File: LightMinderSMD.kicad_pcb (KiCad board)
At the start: 2 copper layers, 49.5 x 23 mm, 39 parts, among them IC2 VN750PSTR-E, J1 Conn_01x06_Male, J2 AVR-ISP-6, J3 Conn_01x03, Q1 Q_NPN_BCE, U1 ATmega328P-AU, U2 LP2951-5.0_SOIC, Y1 Crystal_GND24

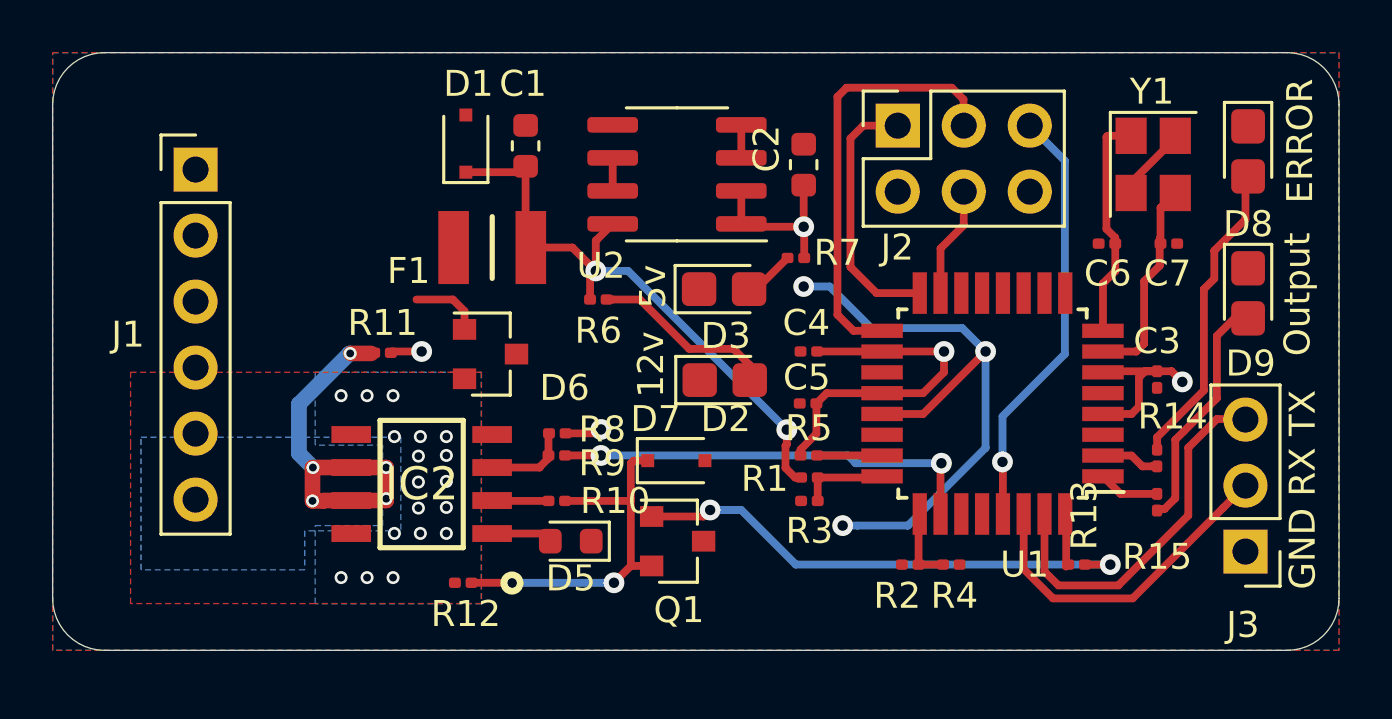
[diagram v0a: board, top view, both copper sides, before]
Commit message: Version 2 PCB fully routed, simulations added
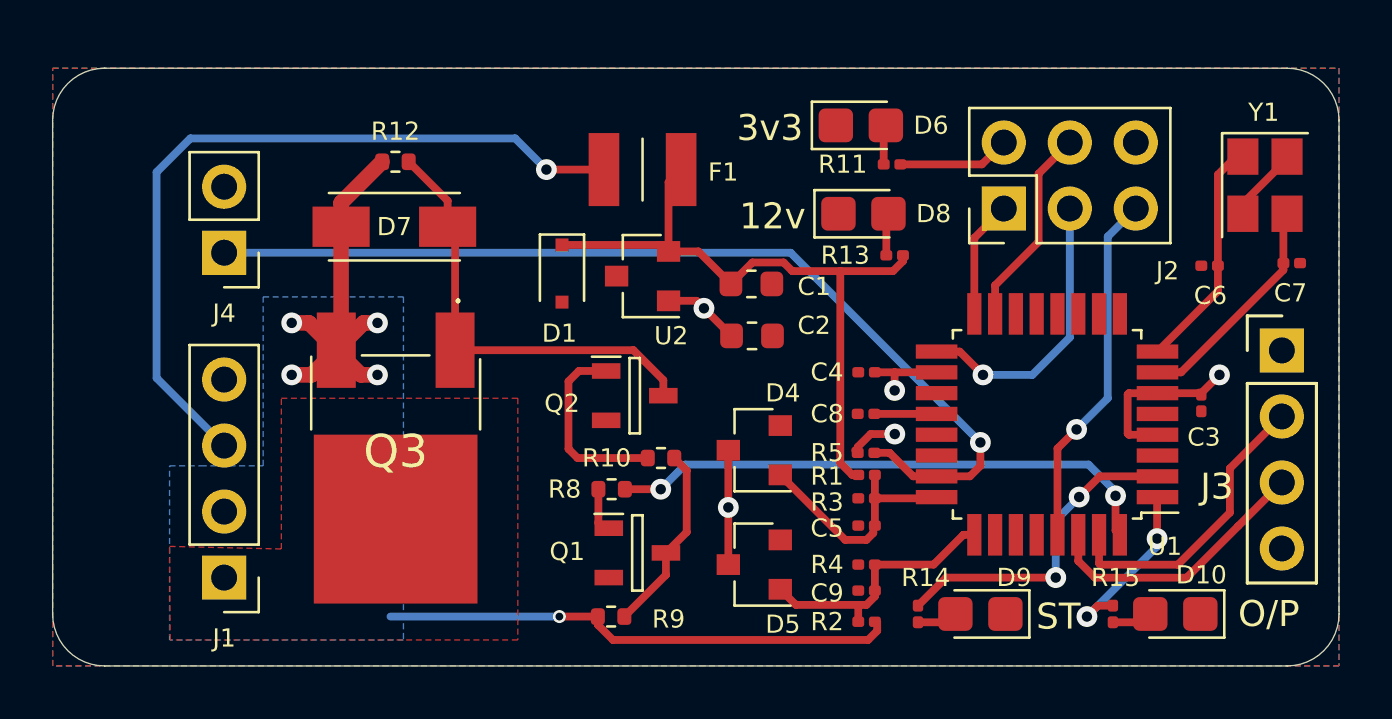
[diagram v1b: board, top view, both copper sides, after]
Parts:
- removed D2, D3: LED, LED_SMD:LED_0805_2012Metric_Castellated
- removed IC2: VN750PSTR-E, SamacSys_Parts:SOIC127P600X175-8N
- removed R6, R7: R, Resistor_SMD:R_0201_0603Metric
- added C8: 100n, Capacitor_SMD:C_0201_0603Metric, F.Cu at (124.3, 84.9)
- added C9: 470nF, Capacitor_SMD:C_0201_0603Metric, F.Cu at (124.3, 91.7)
- added D10: LED, LED_SMD:LED_0805_2012Metric_Castellated, F.Cu at (136.2, 92.6)
- added D4: D_Schottky, Diode_SMD:D_SOT-23_ANK, F.Cu at (120.0, 86.3)
- added J4: Conn_01x02_Female, Connector_PinHeader_2.54mm:PinHeader_1x02_P2.54mm_Vertical, F.Cu at (99.6, 78.7)
- added Q2: Q_NPN_BEC, SamacSys_Parts:SOT95P240X115-3N, F.Cu at (115.4, 84.2)
- added Q3: STD35P6LLF6, SamacSys_Parts:STD35P6LLF6, F.Cu at (106.2, 85.7)
- C1: value 1u -> 10u
- C2: value 4.7u -> 10u
- C5: value 100n -> 470nF
- D5: value D -> D_Schottky; footprint Diode_SMD:D_0603_1608Metric -> Diode_SMD:D_SOT-23_ANK
- D6: value D_TVS -> LED; footprint Diode_SMD:D_SOT-23_NKA -> LED_SMD:LED_0805_2012Metric_Castellated
- D7: value D_Zener -> 20v TVS; footprint Diode_SMD:D_SOD-323F -> SamacSys_Parts:DO-214ACSMA
- J1: value Conn_01x06_Male -> Conn_01x04_Female; footprint Connector_PinHeader_2.54mm:PinHeader_1x06_P2.54mm_Vertical -> Connector_PinHeader_2.54mm:PinHeader_1x04_P2.54mm_Vertical
- J2: footprint Connector_PinSocket_2.54mm:PinSocket_2x03_P2.54mm_Vertical -> Connector_PinHeader_2.54mm:PinHeader_2x03_P2.54mm_Vertical
- J3: value Conn_01x03 -> Conn_01x04; footprint Connector_PinHeader_2.54mm:PinHeader_1x03_P2.54mm_Vertical -> Connector_PinHeader_2.54mm:PinHeader_1x04_P2.54mm_Vertical
- Q1: value Q_NPN_BCE -> Q_NPN_BEC; footprint Package_TO_SOT_SMD:SOT-23 -> SamacSys_Parts:SOT95P240X115-3N
- R1, R2: value 15k -> 18k
- R10, R8: value 10k -> 1k; footprint Resistor_SMD:R_0201_0603Metric -> Resistor_SMD:R_0402_1005Metric
- R11: value 10k -> R
- R12: value 15k -> 10k; footprint Resistor_SMD:R_0201_0603Metric -> Resistor_SMD:R_0402_1005Metric
- R13: value 1k -> R
- R3, R4: value 5k1 -> 1.3k
- R9: footprint Resistor_SMD:R_0201_0603Metric -> Resistor_SMD:R_0402_1005Metric
- U2: value LP2951-5.0_SOIC -> LM3480-3.3; footprint Package_SO:SOIC-8_3.9x4.9mm_P1.27mm -> Package_TO_SOT_SMD:SOT-23
- moved R11 20.9 mm to (125.3, 75.3), turned to 180 degrees
- moved D6 16.7 mm to (124.1, 73.8)
- moved R12 16.4 mm to (106.2, 75.2)
- moved D9 16.1 mm to (128.7, 92.6), turned to 180 degrees
- moved J1 15.7 mm to (99.6, 91.2), turned to 180 degrees
- moved D8 15.0 mm to (124.2, 77.2), turned to 0 degrees
- moved D7 14.1 mm to (106.2, 77.7)
- moved R13 13.8 mm to (125.4, 78.8), turned to 180 degrees
- moved R14 11.0 mm to (126.3, 92.6), turned to 270 degrees
- moved C1 10.2 mm to (119.9, 79.9), turned to 0 degrees
- moved J3 7.87 mm to (140.3, 82.5), turned to 0 degrees
- moved D5 7.12 mm to (120.0, 90.7)
- moved C2 6.88 mm to (119.9, 81.9), turned to 0 degrees
- moved R9 6.54 mm to (114.5, 92.7), turned to 0 degrees
- moved F1 6.52 mm to (115.7, 75.5)
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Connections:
- net /Sheet60CB0BEF/11 renamed /Sheet60CB0BEF/MOSI
- net /Sheet60CB0BEF/12 renamed /Sheet60CB0BEF/MISO
- net /Sheet60CB0BEF/13 renamed /Sheet60CB0BEF/SCK
- C2 pad 1: 5v -> 3v3
- C3 pad 1: 5v -> 3v3
- C4 pad 1: 5v -> 3v3
- C5 pad 1: 5v -> /batt_voltage_ref
- D5 pad 1: Sidelight_GND -> 3v3
- D5 pad 2: Net-(D5-Pad2) -> /dipped_beam_ref
- D6 pad 1: DippedBeam_12v -> Sidelight_GND
- D6 pad 2: Sidelight_GND -> Net-(D6-Pad2)
- D7 pad 1: /Light_Control -> DippedBeam_12v
- D7 pad 2: Sidelight_GND -> Net-(D7-Pad2)
- J1 pad 1: Sidelight_GND -> DippedBeam_Out
- J1 pad 2: /Light_Ref -> DippedBeam_12v
- J1 pad 3: Sidelight_GND -> Sidelight_12v
- J1 pad 4: Sidelight_12v -> Sidelight_GND
- J2 pad 2: 5v -> 3v3
- J3 pad 2: /RX -> /TX
- J3 pad 3: /TX -> /RX
- Q1 pad 2: /Light_Control -> Sidelight_GND
- Q1 pad 3: Sidelight_GND -> Net-(Q1-Pad3)
- R1 pad 2: /Batt_Voltage_Ref -> /batt_voltage_ref
- R10 pad 1: Net-(IC2-Pad2) -> Net-(Q1-Pad3)
- R10 pad 2: /Light_Control -> Net-(Q2-Pad1)
- R11 pad 1: DippedBeam_Out -> 3v3
- R11 pad 2: 5v -> Net-(D6-Pad2)
- R12 pad 2: /Light_Control -> Net-(D7-Pad2)
- R13 pad 1: /Light_Out_Gate -> /12vFused
- R13 pad 2: Net-(Q1-Pad1) -> Net-(D8-Pad2)
- R14 pad 2: Net-(D8-Pad2) -> Net-(D9-Pad2)
- R15 pad 2: Net-(D9-Pad2) -> Net-(D10-Pad2)
- R2 pad 2: /Dipped_Beam_Ref -> /dipped_beam_ref
- R3 pad 1: /Batt_Voltage_Ref -> /batt_voltage_ref
- R4 pad 1: /Dipped_Beam_Ref -> /dipped_beam_ref
- R5 pad 1: 5v -> 3v3
- R5 pad 2: /Light_Ref -> /light_ref
- R8 pad 1: Net-(IC2-Pad3) -> /Light_Out_Logic
- R8 pad 2: 5v -> Net-(Q1-Pad1)
- R9 pad 1: /Status_In -> DippedBeam_12v
- R9 pad 2: Net-(IC2-Pad3) -> Net-(Q1-Pad3)
- U1 pad 18: 5v -> 3v3
- U1 pad 20: 5v -> /Sheet60CB0BEF/aref
- U1 pad 23: /Light_Ref -> /light_ref
- U1 pad 24: /Batt_Voltage_Ref -> /batt_voltage_ref
- U1 pad 25: /Dipped_Beam_Ref -> /dipped_beam_ref
- U1 pad 26: /Status_In -> /Sheet60CB0BEF/A3
- U1 pad 32: /Light_Out_Gate -> /Light_Out_Logic
- U1 pad 4: 5v -> 3v3
- U1 pad 6: 5v -> 3v3
- U2 pad 1: 5v -> 3v3
- U2 pad 2: 5v -> /12vFused
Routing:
- net /light_ref: track 0.00 -> 37.7 mm, vias 0 -> 1
- net DippedBeam_12v: track 0.00 -> 36.2 mm, vias 18 -> 5
- net Sidelight_12v: track 0.00 -> 29.8 mm, vias 0 -> 1
- net 5v: track 29.2 -> 0.00 mm, vias 5 -> 0
- net Sidelight_GND: track 27.6 -> 2.90 mm, vias 3 -> 0
- net 3v3: track 0.00 -> 23.3 mm, vias 0 -> 5
- net /Light_Out_Logic: track 0.00 -> 21.3 mm, vias 0 -> 2
- net Net-(Q1-Pad1): track 20.0 -> 1.78 mm, vias 2 -> 0
- net Net-(D7-Pad2): track 0.00 -> 17.1 mm
- net /Status_In: track 16.6 -> 0.00 mm, vias 2 -> 0
- net DippedBeam_Out: track 14.5 -> 0.00 mm, vias 5 -> 0
- net /Light_Control: track 14.4 -> 0.00 mm, vias 2 -> 0
- net Net-(D8-Pad2): track 12.0 -> 1.63 mm
- net /Error_LED: track 2.26 -> 12.6 mm, vias 0 -> 2
- net /dipped_beam_ref: track 0.00 -> 10.2 mm
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- added copper zone on B.Cu, net 3v3
- added copper zone on F.Cu, net DippedBeam_Out
- removed copper zone on B.Cu, net 5v
- removed copper zone on F.Cu, net DippedBeam_12v
- removed copper zone on B.Cu, net DippedBeam_Out
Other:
- board text added: "12v"
- board text added: "3v3"
- board text added: "O/P"
- board text added: "ST"

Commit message: Finalise PCB, add logo and silk text
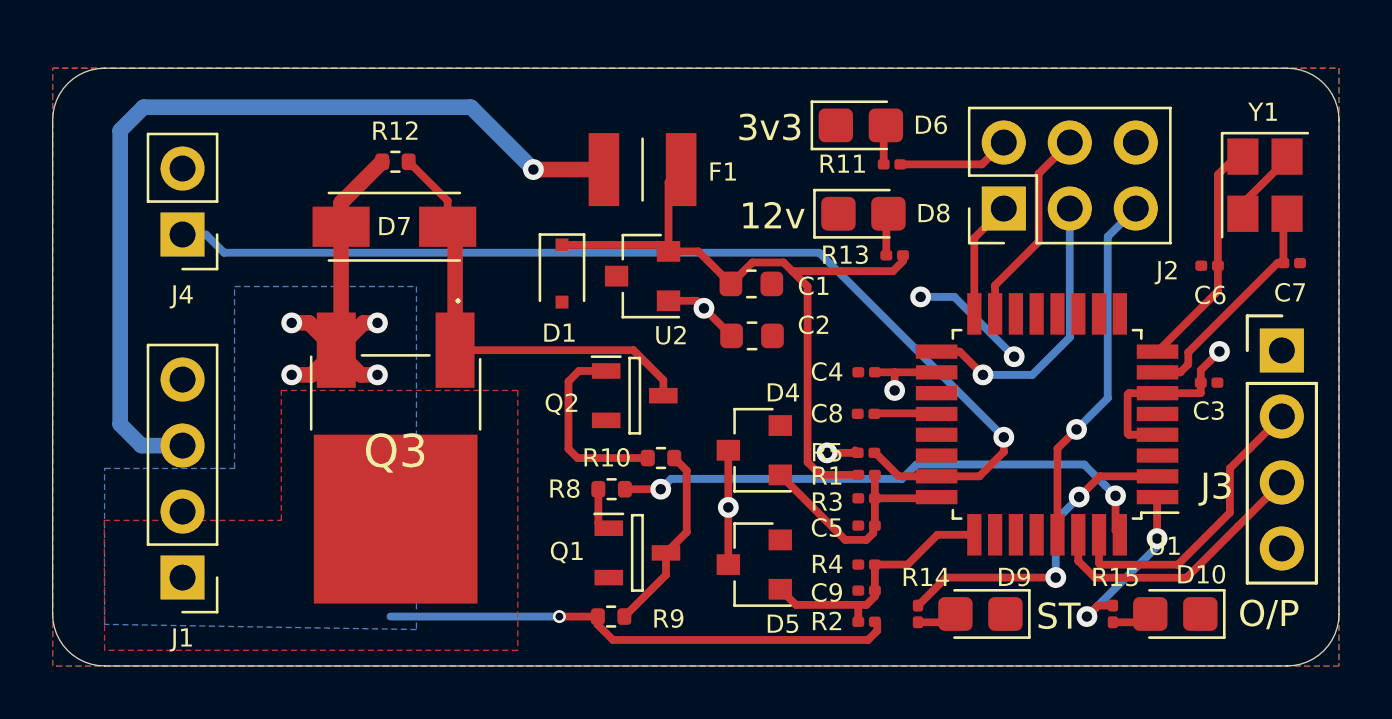
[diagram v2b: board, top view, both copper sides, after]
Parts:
- added G***: LOGO, User_Lib:lightminder_logo, B.Cu at (119.0, 86.3)
- moved J4 1.75 mm to (98.0, 78.0)
- moved J1 1.60 mm to (98.0, 91.2)
- moved C3 0.84 mm to (137.5, 83.7), turned to 0 degrees
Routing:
- net Sidelight_GND: track 2.90 -> 7.46 mm, vias 0 -> 2
- net Sidelight_12v: track 29.8 -> 34.0 mm
- net /light_ref: track 37.7 -> 41.1 mm
- net /12vFused: track 26.2 -> 27.7 mm
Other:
- board text added: "Dip In"
- board text added: "Dip Out"
- board text added: "GND"
- board text added: "ISCP"
- board text added: "Light Sensor"
- board text added: "RX"
- board text added: "Serial Port"
- board text added: "TX"
- board text added: "V+"
- board text added: "v0.3 PROTOTYPE 2021"

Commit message: Version 0.3 prototype - Manufactured
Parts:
- removed D4, D5: D_Schottky, Diode_SMD:D_SOT-23_ANK
- removed the G*** at (119.0, 86.3)
- added G***: LOGO, user:LightMinderLogo2, B.Cu at (115.8, 90.7)
- C3, C4, C5, C6, C7, C8, C9: footprint Capacitor_SMD:C_0201_0603Metric -> Capacitor_SMD:C_0603_1608Metric
- R1, R2, R3, R4, R5: footprint Resistor_SMD:R_0201_0603Metric -> Resistor_SMD:R_0603_1608Metric
- R10, R12, R8, R9: footprint Resistor_SMD:R_0402_1005Metric -> Resistor_SMD:R_0603_1608Metric
- R11, R14, R15: value R -> 100; footprint Resistor_SMD:R_0201_0603Metric -> Resistor_SMD:R_0603_1608Metric
- R13: value R -> 750; footprint Resistor_SMD:R_0201_0603Metric -> Resistor_SMD:R_0603_1608Metric
- moved R5 4.69 mm to (119.9, 84.7)
- moved R4 4.56 mm to (119.8, 90.1)
- moved R3 4.50 mm to (119.9, 87.3)
- moved R2 4.50 mm to (119.8, 92.8)
- moved C6 4.34 mm to (136.8, 74.9), turned to 90 degrees
- moved C3 4.04 mm to (139.8, 80.4)
- moved C4 2.10 mm to (123.7, 81.3)
- moved R8 2.04 mm to (112.5, 88.2), turned to 270 degrees
- moved C8 1.81 mm to (123.7, 83.2)
- moved F1 1.31 mm to (114.4, 75.5)
- moved R1 1.26 mm to (123.8, 86.1)
- moved R13 1.14 mm to (124.3, 79.1), turned to 0 degrees
- moved D8 1.14 mm to (123.1, 77.2)
- moved D6 1.04 mm to (123.1, 73.8)
- moved R10 0.98 mm to (115.4, 86.6)
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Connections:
- U1 pad 10: /Sheet60CB0BEF/6 -> (no net)
- U1 pad 11: /Sheet60CB0BEF/7 -> (no net)
- U1 pad 12: /Sheet60CB0BEF/8 -> (no net)
- U1 pad 13: /Sheet60CB0BEF/9 -> (no net)
- U1 pad 14: /Sheet60CB0BEF/10 -> (no net)
- U1 pad 19: /Sheet60CB0BEF/A6 -> (no net)
- U1 pad 22: /Sheet60CB0BEF/A7 -> (no net)
- U1 pad 26: /Sheet60CB0BEF/A3 -> (no net)
- U1 pad 27: /Sheet60CB0BEF/A4 -> (no net)
- U1 pad 28: /Sheet60CB0BEF/A5 -> (no net)
- U1 pad 9: /Sheet60CB0BEF/5 -> (no net)
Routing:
- net /light_ref: track 41.1 -> 47.9 mm, vias 1 -> 2
- net /12vFused: track 27.7 -> 23.6 mm, vias 0 -> 2
- net /Light_Out_Logic: track 21.2 -> 25.2 mm
- net 3v3: track 23.6 -> 27.2 mm, vias 5 -> 4
- net /dipped_beam_ref: track 10.2 -> 13.5 mm
- net /Light_Out_LED: track 6.89 -> 9.85 mm
- net Sidelight_GND: track 7.46 -> 10.1 mm
- net DippedBeam_12v: track 36.2 -> 37.6 mm, vias 5 -> 6
- net Net-(Q2-Pad1): track 7.41 -> 6.11 mm
- net /Sheet60CB0BEF/aref: track 2.41 -> 3.58 mm
- net /TX: track 11.5 -> 10.5 mm
- net Net-(D9-Pad2): track 1.72 -> 2.68 mm
- net /Sheet60CB0BEF/XTAL2: track 9.02 -> 9.97 mm
- net /Error_LED: track 12.6 -> 13.5 mm
- net /Sheet60CB0BEF/XTAL1: track 8.81 -> 9.57 mm
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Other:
- rule pad_to_mask_clearance: 0.051 -> 0
- board text added: "OUT"
- board text removed: "O/P"

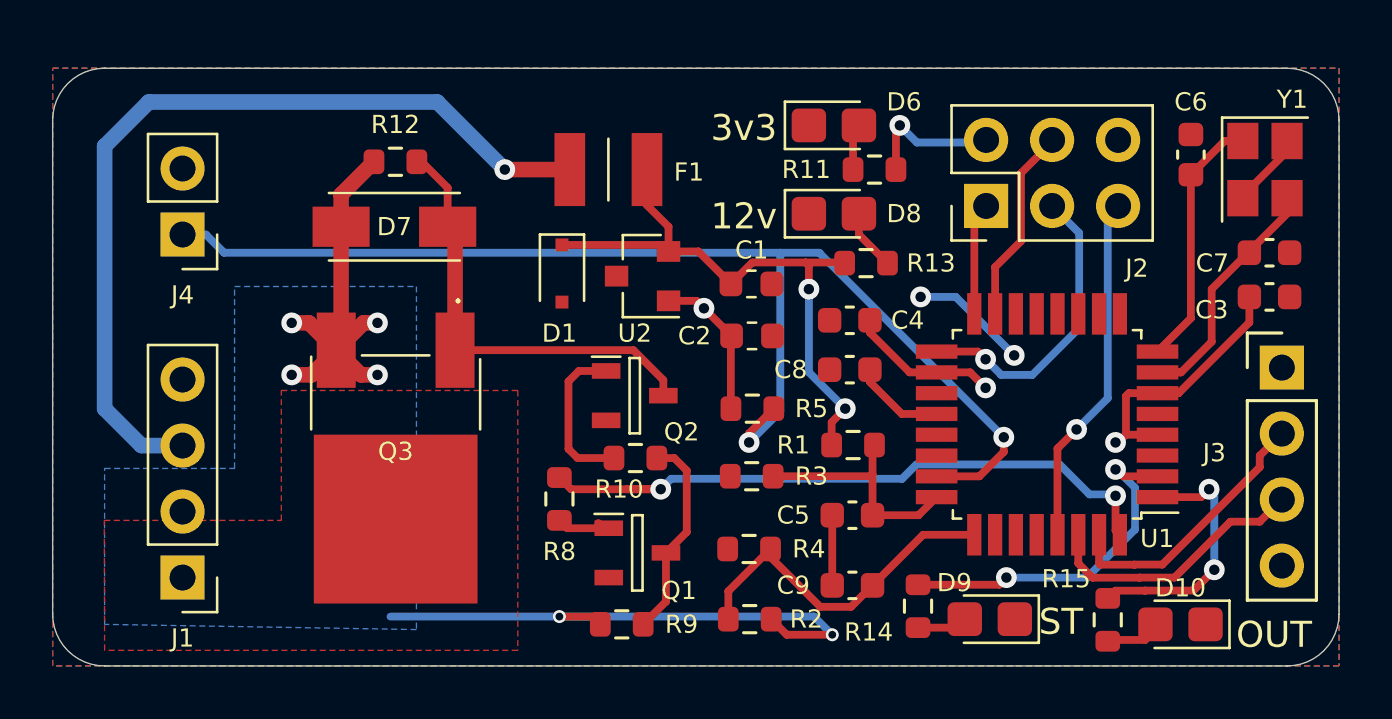
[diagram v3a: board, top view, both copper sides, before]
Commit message: Upgrade to 6.0 and add html bom
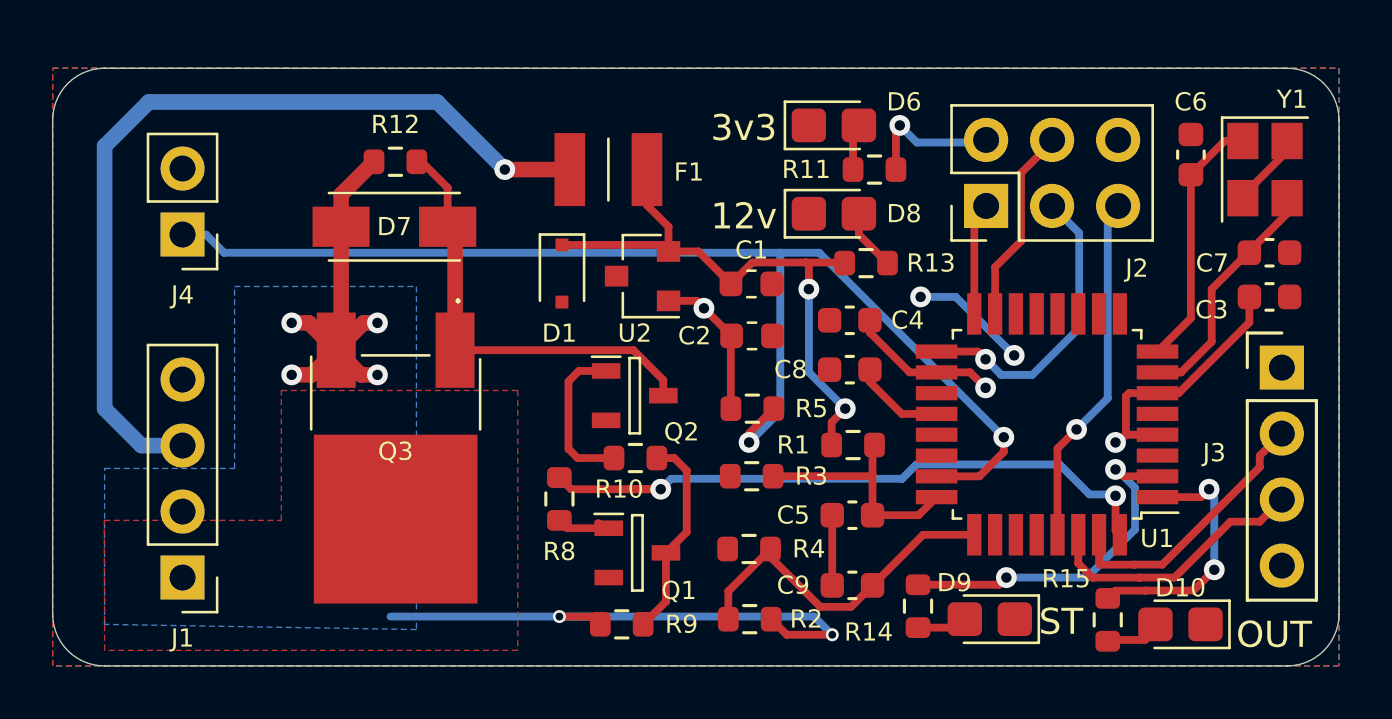
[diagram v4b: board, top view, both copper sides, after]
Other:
- net class BeamPower removed
- net class Default removed

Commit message: Starting V0.4 Updates
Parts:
- added D2: D_Schottky, Diode_SMD:D_0603_1608Metric, F.Cu at (117.4, 79.7)
- moved U2 1.20 mm to (114.5, 79.6)
- moved D1 1.20 mm to (111.4, 79.5)
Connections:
- U1 pad 10: (no net) -> /Error_LED
- U1 pad 11: (no net) -> /Sheet60CB0BEF/7
- U1 pad 12: (no net) -> /Sheet60CB0BEF/8
- U1 pad 13: (no net) -> /Sheet60CB0BEF/9
- U1 pad 14: (no net) -> /Sheet60CB0BEF/10
- U1 pad 19: (no net) -> /Sheet60CB0BEF/A6
- U1 pad 2: /Error_LED -> /Sheet60CB0BEF/4
- U1 pad 22: (no net) -> /Sheet60CB0BEF/A7
- U1 pad 26: (no net) -> /Sheet60CB0BEF/A3
- U1 pad 27: (no net) -> /Sheet60CB0BEF/A4
- U1 pad 28: (no net) -> /Sheet60CB0BEF/A5
- U1 pad 32: /Light_Out_Logic -> /Sheet60CB0BEF/2
- U1 pad 9: (no net) -> /Light_Out_Logic
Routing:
- net 3v3: track 27.2 -> 30.9 mm
- net /Light_Out_Logic: track 25.2 -> 28.1 mm
- net /Error_LED: track 13.5 -> 15.1 mm
- net /12vFused: track 23.6 -> 24.6 mm
